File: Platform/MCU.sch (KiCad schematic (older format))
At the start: 38 parts, among them J10 Conn_01x05, J11 Aardvark Header SPI, J12 Aardvark Header I2C, J13 ESP8266_CONN, J14 Aardvark Header I2C, J4 Conn_01x05, J6 Debug Hdr, J7 Conn_01x05, U3 ATSAMD21E16B-M

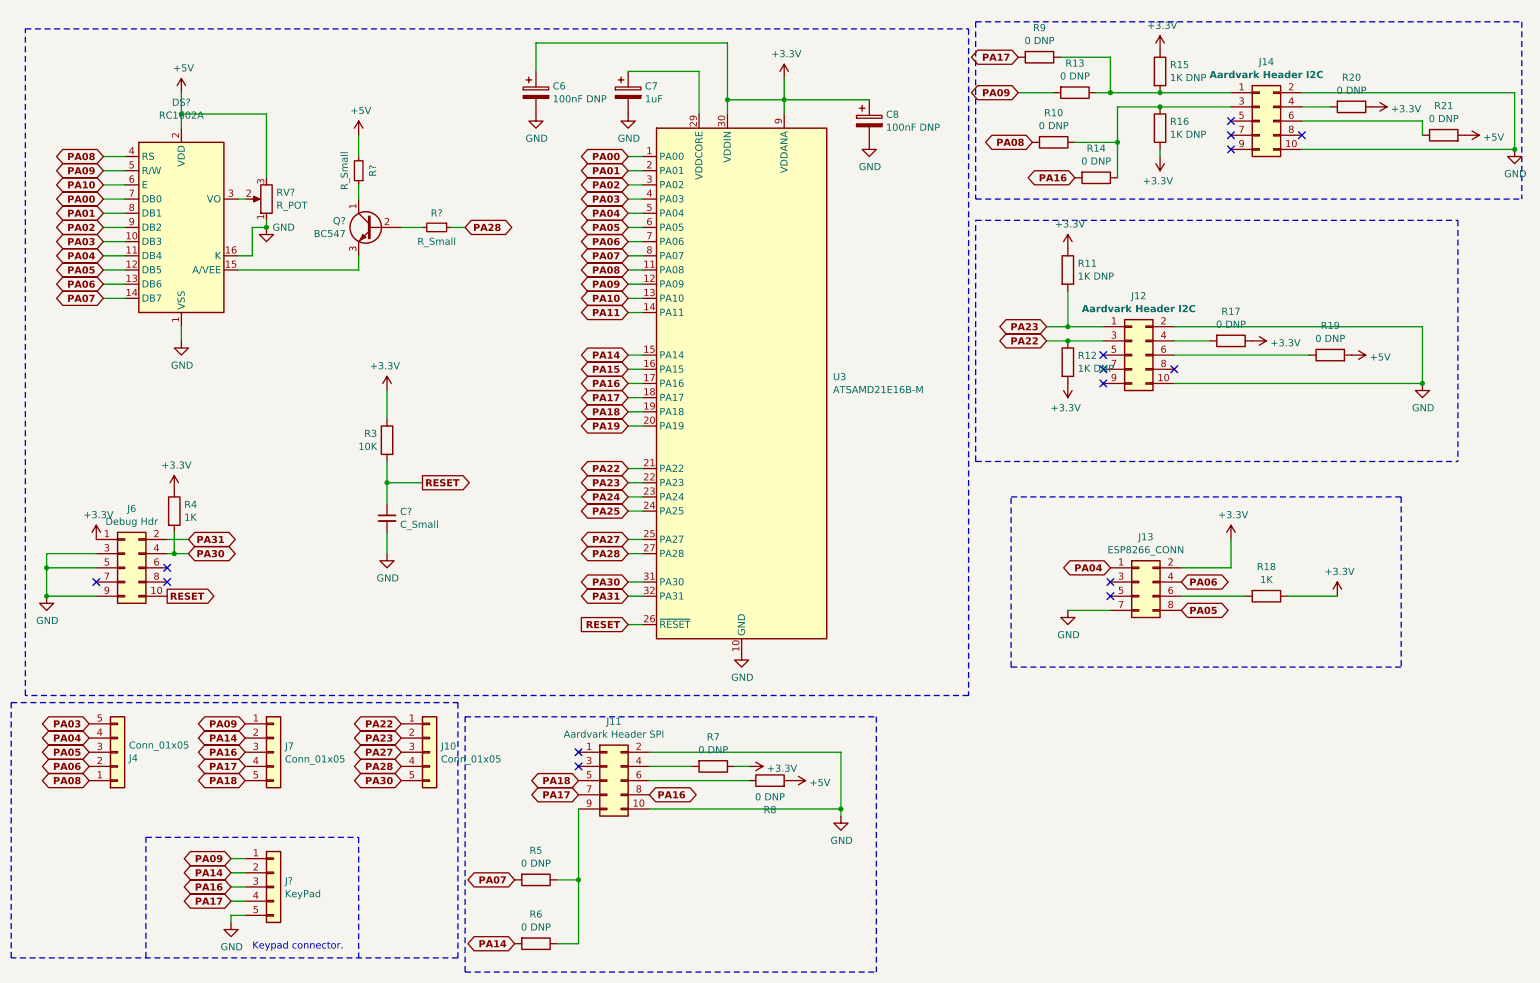
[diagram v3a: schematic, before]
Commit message: updated the schematic as per the latest IO xls.
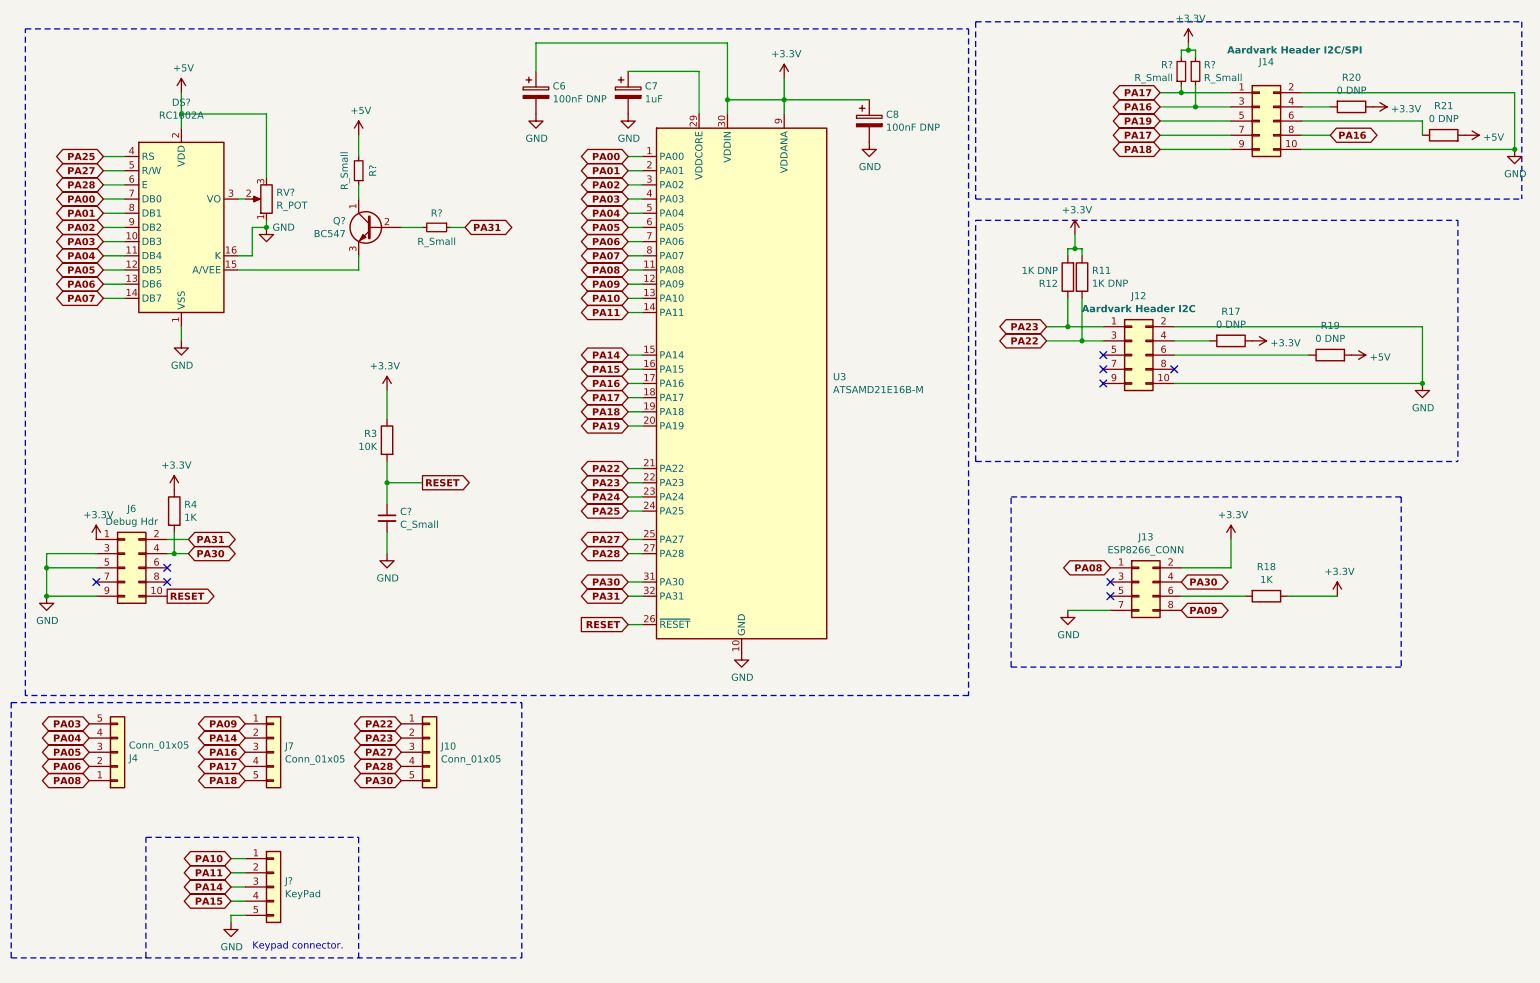
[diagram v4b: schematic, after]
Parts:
- removed J11: Aardvark Header SPI, symbol Connector_Generic:Conn_02x05_Odd_Even
- removed R10, R13, R14, R5, R6, R7, R8, R9: 0 DNP, symbol Device:R
- removed R15, R16: 1K DNP, symbol Device:R
- added R? (x2): R_Small, symbol Device:R_Small
- J14: value Aardvark Header I2C -> Aardvark Header I2C/SPI
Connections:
- net +3V3: now also R?.1, R?.2
- net PA04: no longer J13.1 (Pin_1)
- net PA05: no longer J13.8 (Pin_8)
- net PA06: no longer J13.4 (Pin_4)
- net PA08: now also J13.1 (Pin_1); no longer DS?.4 (RS)
- net PA09: now also J13.8 (Pin_8); no longer DS?.5 (R/W), J?.1 (Pin_1)
- net PA10: now also J?.1 (Pin_1); no longer DS?.6 (E)
- net PA11: now also J?.2 (Pin_2)
- net PA14: now also J?.3 (Pin_3); no longer J?.2 (Pin_2)
- net PA15: now also J?.4 (Pin_4)
- net PA16: now also J14.3 (Pin_3), J14.8 (Pin_8), R?.2; no longer J?.3 (Pin_3)
- net PA17: now also J14.1 (Pin_1), J14.7 (Pin_7), R?.1; no longer J?.4 (Pin_4)
- net PA18: now also J14.9 (Pin_9)
- net PA19: now also J14.5 (Pin_5)
- net PA22: now also R11.2; no longer R12.1
- net PA23: now also R12.1; no longer R11.2
- net PA25: now also DS?.4 (RS)
- net PA27: now also DS?.5 (R/W)
- net PA28: now also DS?.6 (E); no longer R?.1
- net PA30: now also J13.4 (Pin_4)
- net PA31: now also R?.1
- no-connect marks 15 -> 9
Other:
- moved on the sheet: R11, R12

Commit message: Added power input detection circuit.
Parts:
- gave numbers to parts that had none: 9
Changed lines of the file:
@@
 	550  7500 550  5700
 $Comp
-L Connector_Generic:Conn_01x05 J?
+L Connector_Generic:Conn_01x05 J9
 U 1 1 60173DD1
 P 2400 7000
-F 0 "J?" H 2480 7042 50  0000 L CNN
+F 0 "J9" H 2480 7042 50  0000 L CNN
 F 1 "KeyPad" H 2480 6951 50  0000 L CNN
 F 2 "" H 2400 7000 50  0001 C CNN
@@
 $EndComp
 $Comp
-L power:GND #PWR?
+L power:GND #PWR032
 U 1 1 60174F24
 P 2100 7250
-F 0 "#PWR?" H 2100 7000 50  0001 C CNN
+F 0 "#PWR032" H 2100 7000 50  0001 C CNN
 F 1 "GND" H 2105 7077 50  0000 C CNN
 F 2 "" H 2100 7250 50  0001 C CNN
@@
 Keypad connector.
 $Comp
-L Display_Character:RC1602A DS?
+L Display_Character:RC1602A DS1
 U 1 1 6019A893
 P 1750 2350
-F 0 "DS?" H 1750 3231 50  0000 C CNN
+F 0 "DS1" H 1750 3231 50  0000 C CNN
 F 1 "RC1602A" H 1750 3140 50  0000 C CNN
 F 2 "Display:HY1602E" H 1750 1450 50  0001 C CIN
@@
 	1350 2850 1200 2850
 $Comp
-L power:+5V #PWR?
+L power:+5V #PWR026
 U 1 1 601E129D
 P 1750 1400
-F 0 "#PWR?" H 1750 1250 50  0001 C CNN
+F 0 "#PWR026" H 1750 1250 50  0001 C CNN
 F 1 "+5V" H 1765 1573 50  0000 C CNN
 F 2 "" H 1750 1400 50  0001 C CNN
@@
 $EndComp
 $Comp
-L power:GND #PWR?
+L power:GND #PWR029
 U 1 1 601E5E6B
 P 1750 3150
-F 0 "#PWR?" H 1750 2900 50  0001 C CNN
+F 0 "#PWR029" H 1750 2900 50  0001 C CNN
 F 1 "GND" H 1755 2977 50  0000 C CNN
 F 2 "" H 1750 3150 50  0001 C CNN
@@
 	1350 1850 1200 1850
 $Comp
-L Device:R_Small R?
+L Device:R_Small R10
 U 1 1 6020D43B
 P 3550 2350
-F 0 "R?" V 3450 2350 50  0000 C CNN
+F 0 "R10" V 3450 2350 50  0000 C CNN
 F 1 "R_Small" V 3650 2350 50  0000 C CNN
 F 2 "" H 3550 2350 50  0001 C CNN
@@
 $EndComp
 $Comp
-L power:GND #PWR?
+L power:GND #PWR041
 U 1 1 60207B70
 P 2350 2350
-F 0 "#PWR?" H 2350 2100 50  0001 C CNN
+F 0 "#PWR041" H 2350 2100 50  0001 C CNN
 F 1 "GND" H 2550 2350 50  0000 R CNN
 F 2 "" H 2350 2350 50  0001 C CNN
@@
 $EndComp
 $Comp
-L power:+5V #PWR?
+L power:+5V #PWR042
 U 1 1 601A2CF8
 P 3000 1700
-F 0 "#PWR?" H 3000 1550 50  0001 C CNN
+F 0 "#PWR042" H 3000 1550 50  0001 C CNN
 F 1 "+5V" H 3015 1873 50  0000 C CNN
 F 2 "" H 3000 1700 50  0001 C CNN
@@
 $EndComp
 $Comp
-L Device:R_POT RV?
+L Device:R_POT RV2
 U 1 1 601A87D3
 P 2350 2150
-F 0 "RV?" H 2280 2104 50  0000 R CNN
+F 0 "RV2" H 2280 2104 50  0000 R CNN
 F 1 "R_POT" H 2280 2195 50  0000 R CNN
 F 2 "" H 2350 2150 50  0001 C CNN
@@
 Connection ~ 2350 2350
 $Comp
-L Transistor_BJT:BC547 Q?
+L Transistor_BJT:BC547 Q1
 U 1 1 601C0547
 P 3100 2350
-F 0 "Q?" H 3291 2396 50  0000 L CNN
+F 0 "Q1" H 3291 2396 50  0000 L CNN
 F 1 "BC547" H 3291 2305 50  0000 L CNN
 F 2 "Package_TO_SOT_THT:TO-92_Inline" H 3300 2275 50  0001 L CIN
@@
 $EndComp
 $Comp
-L Device:R_Small R?
+L Device:R_Small R9
 U 1 1 601C3595
 P 3000 1950
-F 0 "R?" V 2900 1950 50  0000 C CNN
+F 0 "R9" V 2900 1950 50  0000 C CNN
 F 1 "R_Small" V 3100 1950 50  0000 C CNN
 F 2 "" H 3000 1950 50  0001 C CNN
@@
 	3300 2350 3450 2350
 $Comp
-L Device:C_Small C?
+L Device:C_Small C14
 U 1 1 601CEA06
 P 3200 4400
-F 0 "C?" H 3292 4446 50  0000 L CNN
+F 0 "C14" H 3292 4446 50  0000 L CNN
 F 1 "C_Small" H 3292 4355 50  0000 L CNN
 F 2 "" H 3200 4400 50  0001 C CNN
@@
 $EndComp
 $Comp
-L power:GND #PWR?
+L power:GND #PWR043
 U 1 1 601CEDC7
 P 3200 4650
-F 0 "#PWR?" H 3200 4400 50  0001 C CNN
+F 0 "#PWR043" H 3200 4400 50  0001 C CNN
 F 1 "GND" H 3205 4477 50  0000 C CNN
 F 2 "" H 3200 4650 50  0001 C CNN
@@
 	9650 1700 9850 1700
 $Comp
-L Device:R_Small R?
+L Device:R_Small R14
 U 1 1 60696FEF
 P 8900 1250
-F 0 "R?" H 8959 1296 50  0000 L CNN
+F 0 "R14" H 8959 1296 50  0000 L CNN
 F 1 "R_Small" H 8959 1205 50  0000 L CNN
 F 2 "" H 8900 1250 50  0001 C CNN
@@
 $EndComp
 $Comp
-L Device:R_Small R?
+L Device:R_Small R13
 U 1 1 6069757B
 P 8800 1250
-F 0 "R?" H 8741 1204 50  0000 R CNN
+F 0 "R13" H 8741 1204 50  0000 R CNN
 F 1 "R_Small" H 8741 1295 50  0000 R CNN
 F 2 "" H 8800 1250 50  0001 C CNN

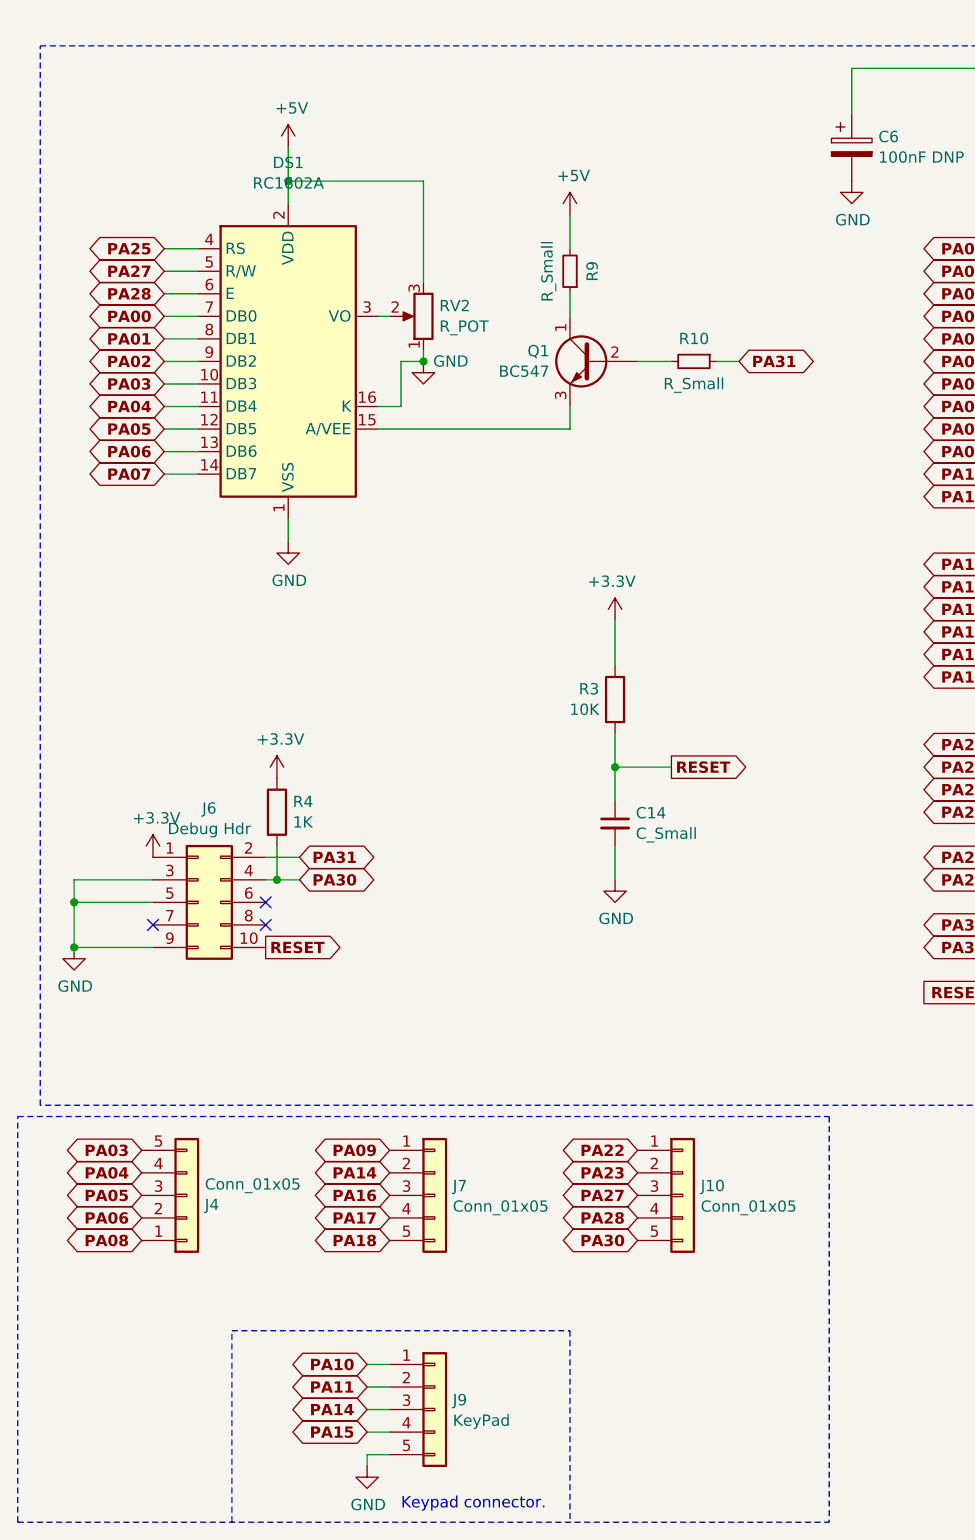
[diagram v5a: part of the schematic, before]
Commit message: added 20 pin header for LED interface.
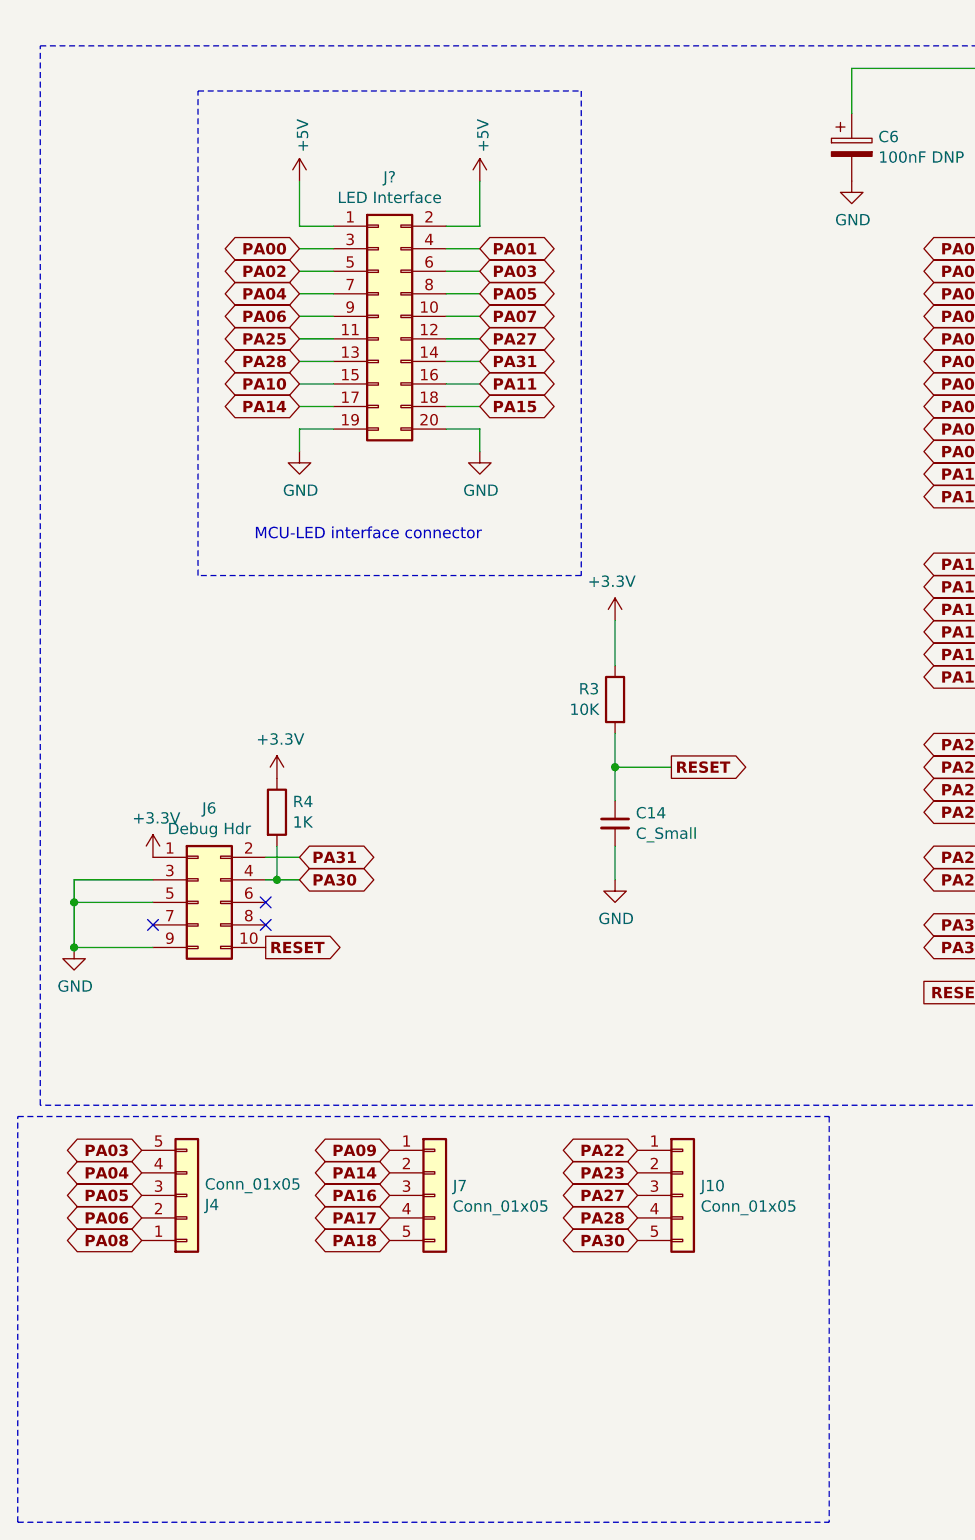
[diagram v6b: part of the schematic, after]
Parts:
- removed DS1: RC1602A, Display:HY1602E, symbol Display_Character:RC1602A
- removed J9: KeyPad, symbol Connector_Generic:Conn_01x05
- removed Q1: BC547, Package_TO_SOT_THT:TO-92_Inline, symbol Transistor_BJT:BC547
- removed R10, R9: R_Small, symbol Device:R_Small
- removed RV2: R_POT, symbol Device:R_POT
- added J?: LED Interface, symbol Connector_Generic:Conn_02x10_Odd_Even
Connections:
- net +5V: now also J?.1 (Pin_1), J?.2 (Pin_2)
- net GND: now also J?.19 (Pin_19), J?.20 (Pin_20)
- net PA00: now also J?.3 (Pin_3)
- net PA01: now also J?.4 (Pin_4)
- net PA02: now also J?.5 (Pin_5)
- net PA03: now also J?.6 (Pin_6)
- net PA04: now also J?.7 (Pin_7)
- net PA05: now also J?.8 (Pin_8)
- net PA06: now also J?.9 (Pin_9)
- net PA07: now also J?.10 (Pin_10)
- net PA10: now also J?.15 (Pin_15)
- net PA11: now also J?.16 (Pin_16)
- net PA14: now also J?.17 (Pin_17)
- net PA15: now also J?.18 (Pin_18)
- net PA25: now also J?.11 (Pin_11)
- net PA27: now also J?.12 (Pin_12)
- net PA28: now also J?.13 (Pin_13)
- net PA31: now also J?.14 (Pin_14)
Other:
- note added: "MCU-LED interface connector"
- note removed: "Keypad connector."
